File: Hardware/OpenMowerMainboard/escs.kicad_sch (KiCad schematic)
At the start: 46 parts, among them J15 Conn_02x02_Female, J24 Conn_01x06_Female, J25 Conn_02x02_Female, J26 Conn_01x06_Female, J27 Conn_02x02_Female, J28 Conn_01x05_Female, J29 Conn_01x05_Female, J30 Conn_01x09_Female, J31 Conn_02x02_Female, J32 Conn_01x06_Female, J33 Conn_02x02_Female, J34 Conn_01x06_Female, J35 Conn_02x02_Female, J36 Conn_01x05_Female, J37 Conn_01x05_Female, J38 Conn_01x09_Female, J39 Conn_02x02_Female, J40 Conn_01x06_Female, J41 Conn_02x02_Female, J42 Conn_01x06_Female, J43 Conn_02x02_Female, J44 Conn_01x05_Female, J45 Conn_01x05_Female, J46 Conn_01x09_Female, U4 xESC2, U5 xESC2, U6 xESC2

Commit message: BOM changes
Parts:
- C2, C3, C4, C6, C7, C8: Digikey (none) -> 399-6654-1-ND
- D10, D11, D12, D18, D19, D20, D4, D5, D6, D7, D8, D9, JP6, U4, U5, U6: DNP (none) -> Y
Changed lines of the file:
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@@
+      (effects (font (size 1.27 1.27)) hide)
+    )
+    (property "DNP" "Y" (id 5) (at 265.43 38.1 0)
       (effects (font (size 1.27 1.27)) hide)
     )
@@
     )
     (property "Config" "do not place" (id 4) (at 100.33 116.205 0)
+      (effects (font (size 1.27 1.27)) hide)
+    )
+    (property "DNP" "Y" (id 5) (at 100.33 116.205 0)
       (effects (font (size 1.27 1.27)) hide)
     )
@@
     )
     (property "Config" "do not place" (id 4) (at 255.905 38.1 0)
+      (effects (font (size 1.27 1.27)) hide)
+    )
+    (property "DNP" "Y" (id 5) (at 255.905 38.1 0)
       (effects (font (size 1.27 1.27)) hide)
     )
@@
       (effects (font (size 1.27 1.27)) hide)
     )
+    (property "DNP" "Y" (id 5) (at 133.35 38.1 0)
+      (effects (font (size 1.27 1.27)) hide)
+    )
     (pin "1")
     (pin "2")
@@
       (effects (font (size 1.27 1.27)) hide)
     )
+    (property "Digikey" "399-6654-1-ND" (id 7) (at 189.865 41.91 0)
+      (effects (font (size 1.27 1.27)) hide)
+    )
     (pin "1")
     (pin "2")
@@
     )
     (property "Config" "do not place" (id 4) (at 231.14 68.58 0)
+      (effects (font (size 1.27 1.27)) hide)
+    )
+    (property "DNP" "Y" (id 5) (at 231.14 68.58 0)
       (effects (font (size 1.27 1.27)) hide)
     )
@@
       (effects (font (size 1.27 1.27)) hide)
     )
+    (property "DNP" "Y" (id 5) (at 114.3 38.1 0)
+      (effects (font (size 1.27 1.27)) hide)
+    )
     (pin "1")
     (pin "2")
@@
       (effects (font (size 1.27 1.27)) hide)
     )
+    (property "DNP" "Y" (id 5) (at 36.195 99.695 0)
+      (effects (font (size 1.27 1.27)) hide)
+    )
     (pin "1")
     (pin "2")
@@
       (effects (font (size 1.27 1.27)) hide)
     )
+    (property "DNP" "Y" (id 5) (at 123.825 38.1 0)
+      (effects (font (size 1.27 1.27)) hide)
+    )
     (pin "1")
     (pin "2")
@@
     )
     (property "Config" "do not place" (id 4) (at 183.515 123.19 0)
+      (effects (font (size 1.27 1.27)) hide)
+    )
+    (property "DNP" "Y" (id 5) (at 183.515 123.19 0)
       (effects (font (size 1.27 1.27)) hide)
     )
@@
     )
     (property "Config" "do not place" (id 4) (at 88.9 68.58 0)
+      (effects (font (size 1.27 1.27)) hide)
+    )
+    (property "DNP" "Y" (id 5) (at 88.9 68.58 0)
       (effects (font (size 1.27 1.27)) hide)
     )
@@
       (effects (font (size 1.27 1.27)) hide)
     )
+    (property "DNP" "Y" (id 5) (at 156.21 153.67 0)
+      (effects (font (size 1.27 1.27)) hide)
+    )
     (pin "1")
     (pin "10")
@@
       (effects (font (size 1.27 1.27)) hide)
     )
+    (property "DNP" "Y" (id 5) (at 202.565 123.19 0)
+      (effects (font (size 1.27 1.27)) hide)
+    )
     (pin "1")
     (pin "2")
@@
       (effects (font (size 1.27 1.27)) hide)
     )
+    (property "DNP" "Y" (id 5) (at 274.955 38.1 0)
+      (effects (font (size 1.27 1.27)) hide)
+    )
     (pin "1")
     (pin "2")
@@
     )
     (property "Stock_PN" "CP-TH-220uF-63V" (id 6) (at 120.015 128.27 0)
+      (effects (font (size 1.27 1.27)) hide)
+    )
+    (property "Digikey" "399-6654-1-ND" (id 7) (at 120.015 128.27 0)
       (effects (font (size 1.27 1.27)) hide)
     )
@@
       (effects (font (size 1.27 1.27)) hide)
     )
+    (property "Digikey" "399-6654-1-ND" (id 7) (at 195.58 41.275 0)
+      (effects (font (size 1.27 1.27)) hide)
+    )
     (pin "1")
     (pin "2")
@@
     )
     (property "Stock_PN" "CP-TH-220uF-63V" (id 6) (at 47.625 45.085 0)
+      (effects (font (size 1.27 1.27)) hide)
+    )
+    (property "Digikey" "399-6654-1-ND" (id 7) (at 47.625 45.085 0)
       (effects (font (size 1.27 1.27)) hide)
     )
@@
     )
     (property "Config" "do not place" (id 4) (at 175.26 31.115 0)
+      (effects (font (size 1.27 1.27)) hide)
+    )
+    (property "DNP" "Y" (id 5) (at 175.26 31.115 0)
       (effects (font (size 1.27 1.27)) hide)
     )
@@
       (effects (font (size 1.27 1.27)) hide)
     )
+    (property "DNP" "Y" (id 5) (at 32.385 31.115 0)
+      (effects (font (size 1.27 1.27)) hide)
+    )
     (pin "1")
     (pin "2")
@@
     )
     (property "Stock_PN" "CP-TH-220uF-63V" (id 6) (at 114.3 128.905 0)
+      (effects (font (size 1.27 1.27)) hide)
+    )
+    (property "Digikey" "399-6654-1-ND" (id 7) (at 114.3 128.905 0)
       (effects (font (size 1.27 1.27)) hide)
     )
@@
       (effects (font (size 1.27 1.27)) hide)
     )
+    (property "DNP" "Y" (id 5) (at 193.04 123.19 0)
+      (effects (font (size 1.27 1.27)) hide)
+    )
     (pin "1")
     (pin "2")
@@
       (effects (font (size 1.27 1.27)) hide)
     )
+    (property "Digikey" "399-6654-1-ND" (id 7) (at 53.34 45.085 0)
+      (effects (font (size 1.27 1.27)) hide)
+    )

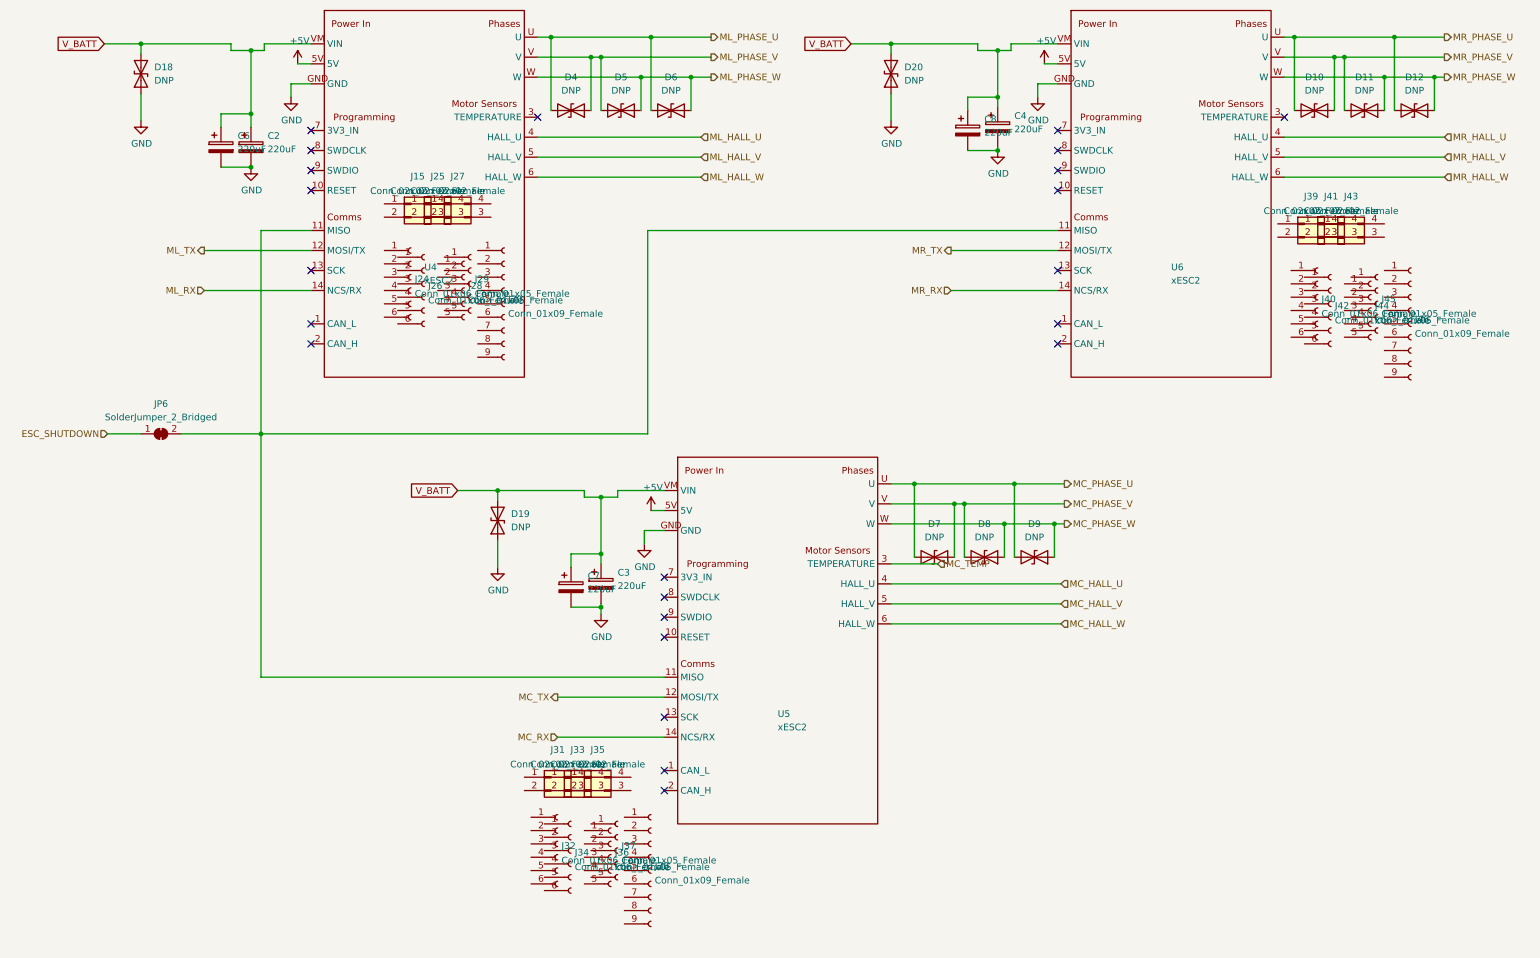
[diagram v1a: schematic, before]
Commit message: fix: fixed ERC/DRC errors, removed LM2596S
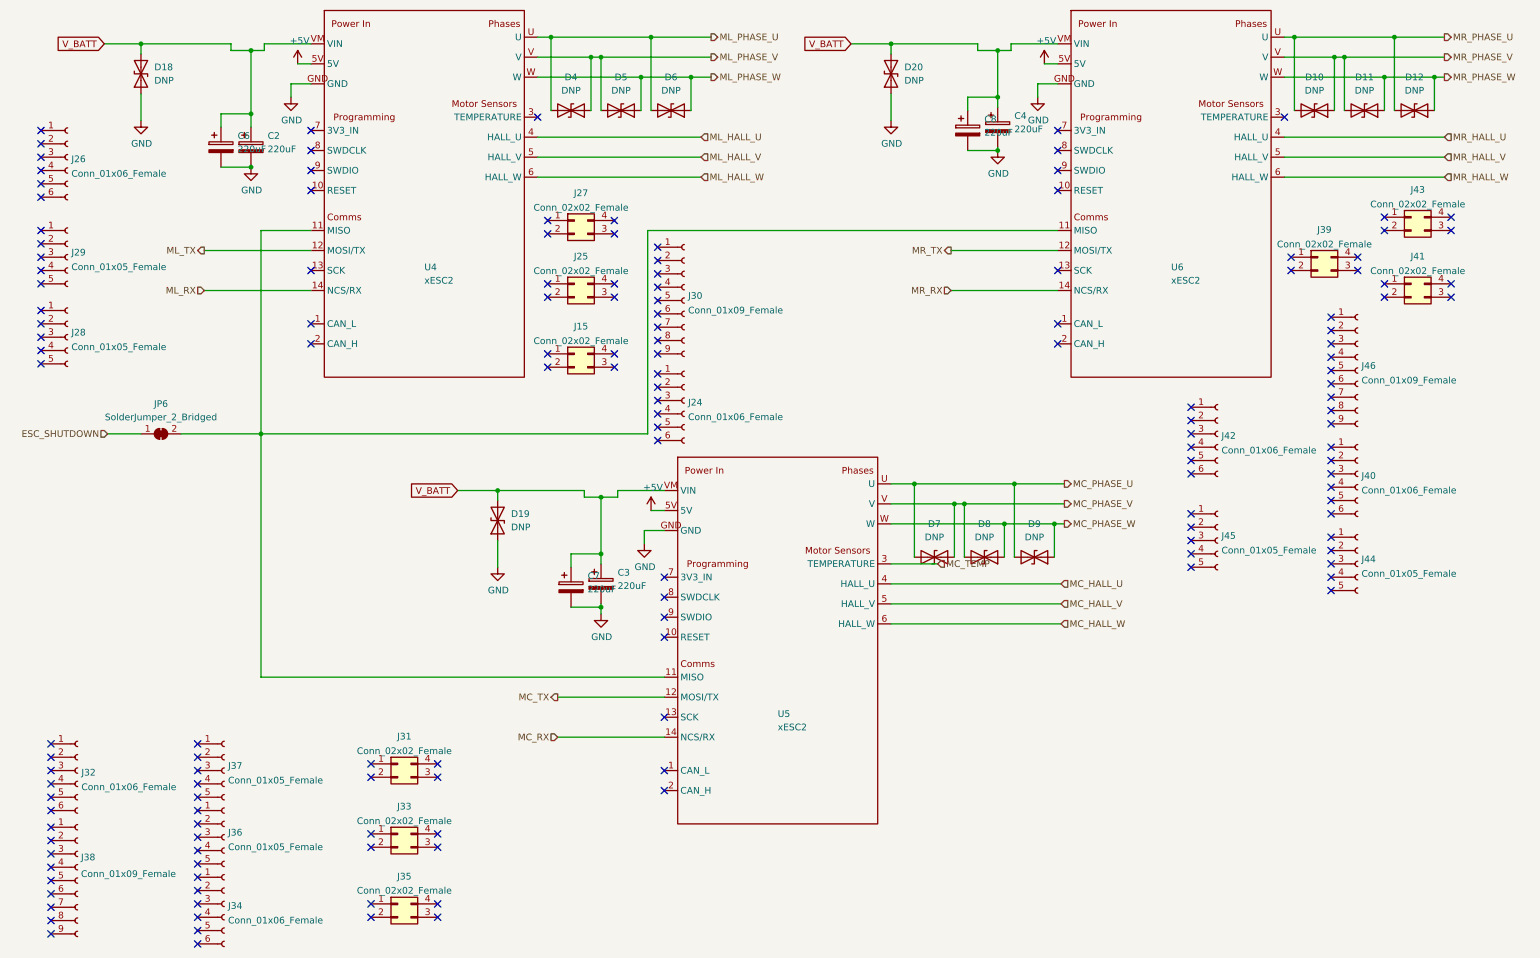
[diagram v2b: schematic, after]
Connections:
- no-connect marks 23 -> 152
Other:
- moved on the sheet: J15, J24, J25, J26, J27, J28, J29, J30, J31, J32, J33, J34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

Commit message: feat: remove C4 from board (no space)
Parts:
- C4: now left out of the parts list
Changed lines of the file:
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@@
   )
   (symbol (lib_id "Device:C_Polarized") (at 195.58 41.275 0) (unit 1)
-    (in_bom yes) (on_board yes) (fields_autoplaced)
+    (in_bom no) (on_board no) (fields_autoplaced)
     (property "Reference" "C4" (id 0) (at 198.755 39.1159 0)
       (effects (font (size 1.27 1.27)) (justify left))

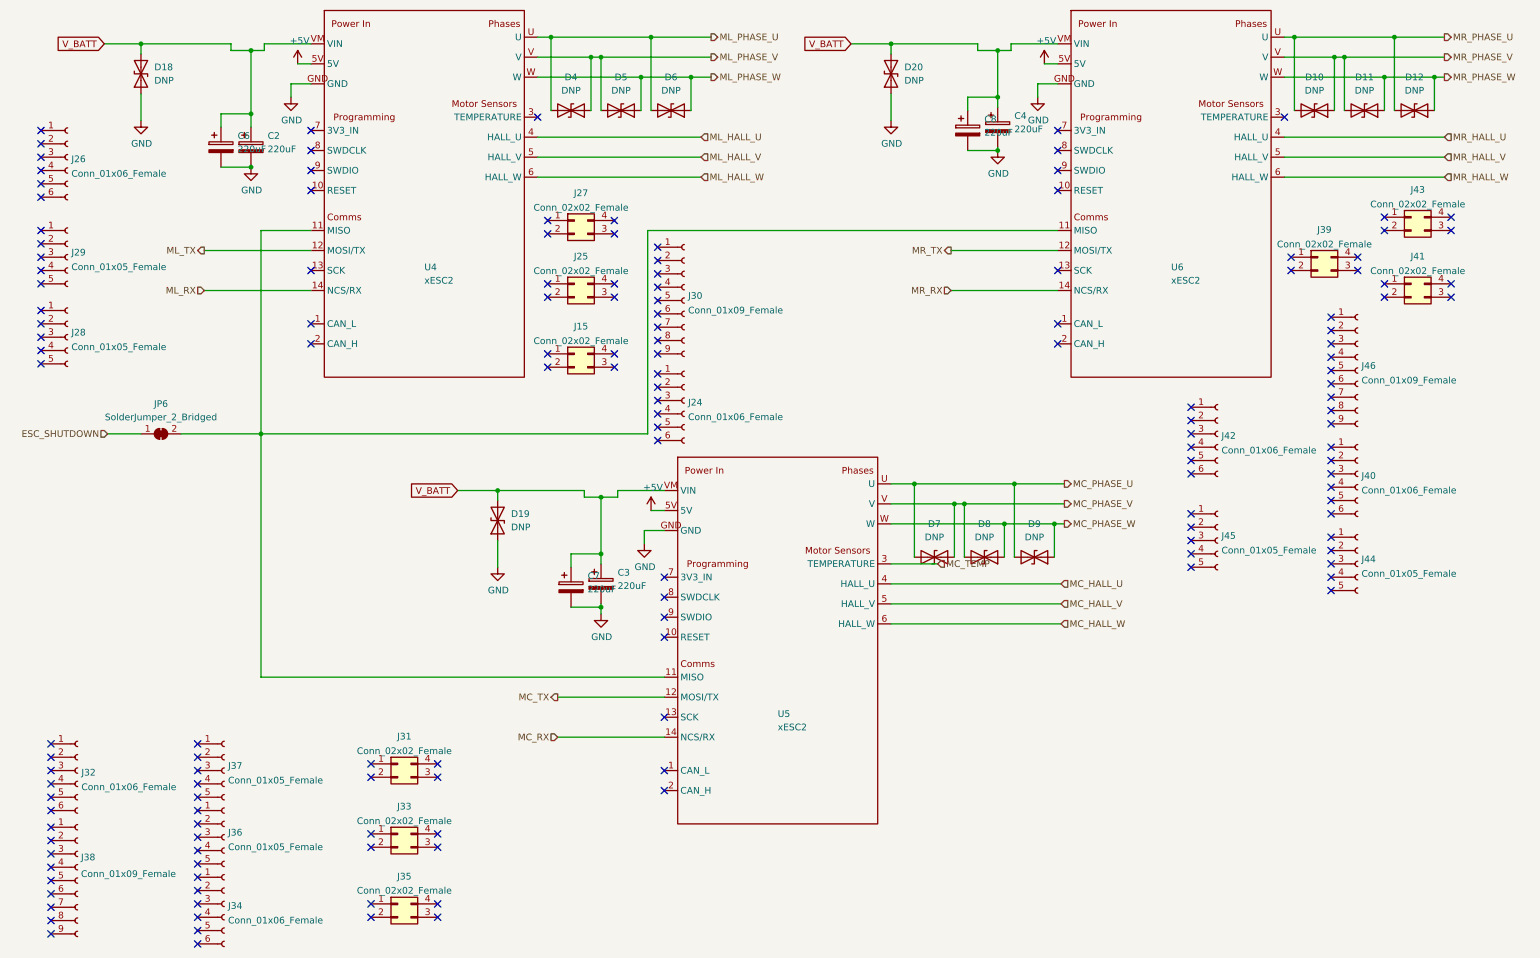
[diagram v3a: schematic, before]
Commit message: fix: exclude C3, C6 from BOM
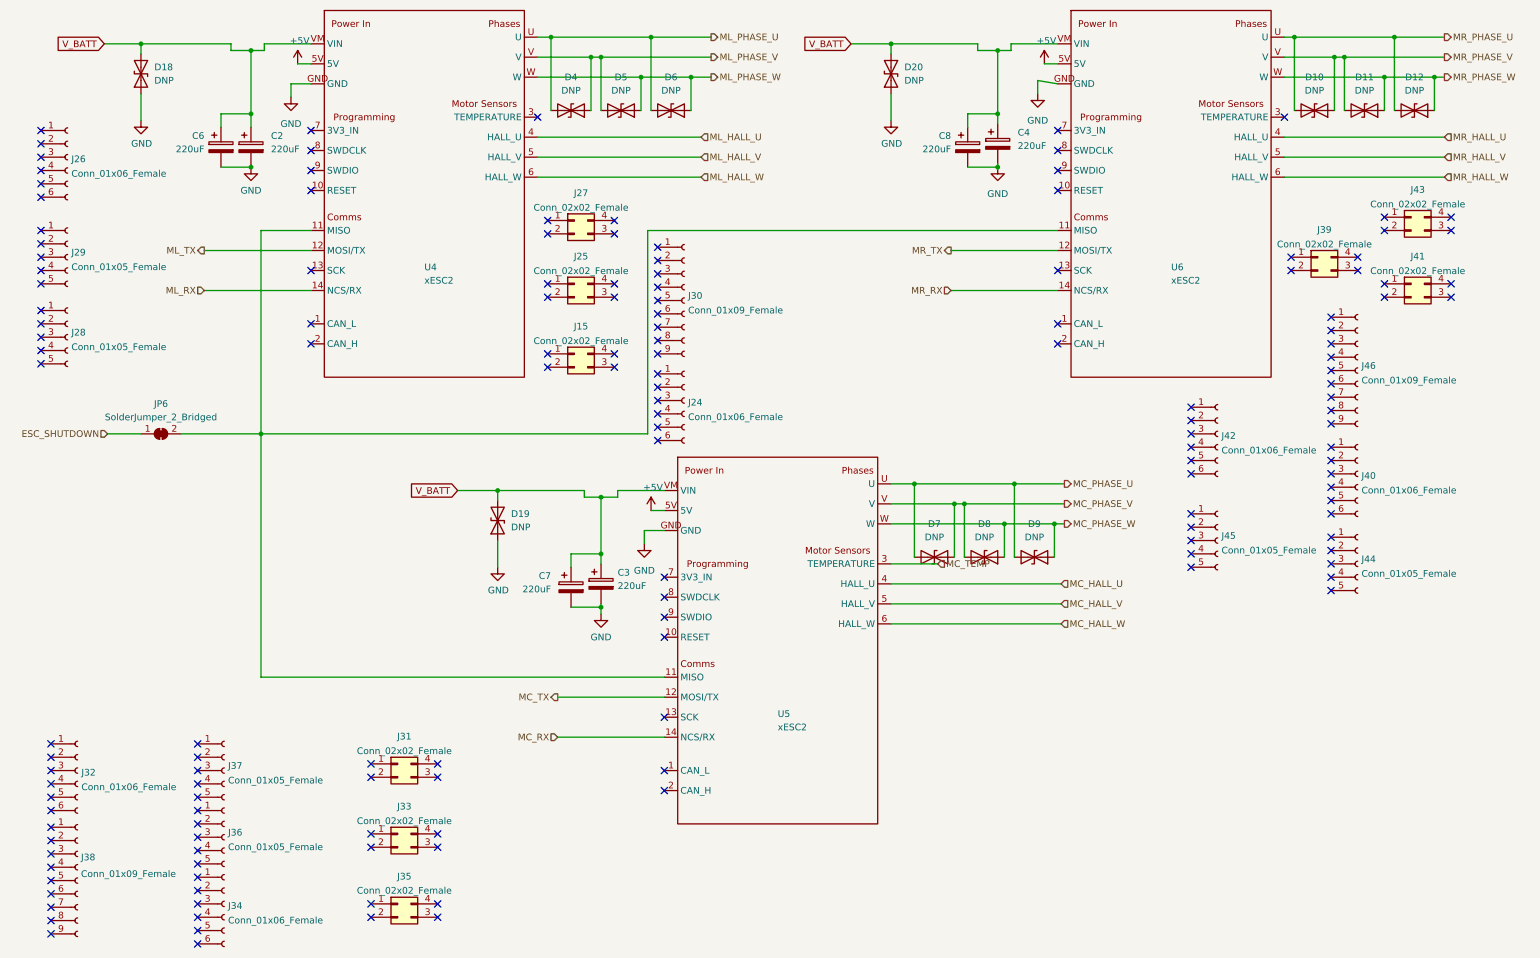
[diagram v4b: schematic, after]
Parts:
- C3, C6: now left out of the parts list
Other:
- moved on the sheet: C4, C8

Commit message: feat(bom): update LCSC codes
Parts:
- C3, C4, C6: Config (none) -> do not place
- J15, J25, J27, J31, J33, J35, J39, J41, J43: LCSC C239342 -> C2935982
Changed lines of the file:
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@@
       (effects (font (size 1.27 1.27)) hide)
     )
-    (property "LCSC" "C239342" (id 4) (at 81.28 162.56 0)
+    (property "LCSC" "C2935982" (id 4) (at 81.28 162.56 0)
       (effects (font (size 1.27 1.27)) hide)
     )
@@
       (effects (font (size 1.27 1.27)) hide)
     )
-    (property "LCSC" "C239342" (id 4) (at 114.935 84.455 0)
+    (property "LCSC" "C2935982" (id 4) (at 114.935 84.455 0)
       (effects (font (size 1.27 1.27)) hide)
     )
@@
       (effects (font (size 1.27 1.27)) hide)
     )
-    (property "LCSC" "C239342" (id 4) (at 274.32 58.42 0)
+    (property "LCSC" "C2935982" (id 4) (at 274.32 58.42 0)
       (effects (font (size 1.27 1.27)) hide)
     )
@@
       (effects (font (size 1.27 1.27)) hide)
     )
-    (property "LCSC" "C239342" (id 4) (at 274.32 71.12 0)
+    (property "LCSC" "C2935982" (id 4) (at 274.32 71.12 0)
       (effects (font (size 1.27 1.27)) hide)
     )
@@
       (effects (font (size 1.27 1.27)) hide)
     )
-    (property "LCSC" "C239342" (id 4) (at 114.935 71.12 0)
+    (property "LCSC" "C2935982" (id 4) (at 114.935 71.12 0)
       (effects (font (size 1.27 1.27)) hide)
     )
@@
       (effects (font (size 1.27 1.27)) hide)
     )
+    (property "Config" "do not place" (id 8) (at 120.015 128.27 0)
+      (effects (font (size 1.27 1.27)) hide)
+    )
     (pin "1")
     (pin "2")
@@
       (effects (font (size 1.27 1.27)) hide)
     )
-    (property "LCSC" "C239342" (id 4) (at 256.54 66.04 0)
+    (property "LCSC" "C2935982" (id 4) (at 256.54 66.04 0)
       (effects (font (size 1.27 1.27)) hide)
     )
@@
     )
     (property "Digikey" "399-6654-1-ND" (id 7) (at 195.58 44.45 0)
+      (effects (font (size 1.27 1.27)) hide)
+    )
+    (property "Config" "do not place" (id 8) (at 195.58 44.45 0)
       (effects (font (size 1.27 1.27)) hide)
     )
@@
       (effects (font (size 1.27 1.27)) hide)
     )
+    (property "Config" "do not place" (id 8) (at 47.625 45.085 0)
+      (effects (font (size 1.27 1.27)) hide)
+    )
     (pin "1")
     (pin "2")
@@
       (effects (font (size 1.27 1.27)) hide)
     )
-    (property "LCSC" "C239342" (id 4) (at 81.28 175.895 0)
+    (property "LCSC" "C2935982" (id 4) (at 81.28 175.895 0)
       (effects (font (size 1.27 1.27)) hide)
     )
@@
       (effects (font (size 1.27 1.27)) hide)
     )
-    (property "LCSC" "C239342" (id 4) (at 114.935 59.055 0)
+    (property "LCSC" "C2935982" (id 4) (at 114.935 59.055 0)
       (effects (font (size 1.27 1.27)) hide)
     )
@@
       (effects (font (size 1.27 1.27)) hide)
     )
-    (property "LCSC" "C239342" (id 4) (at 81.28 189.23 0)
-      (effects (font (size 1.27 1.27)) hide)
-    )
+    (property "LCSC" "C2935982" (id 4) (at 81.28 189.23 0)
+      (effects (font (size 1.27 1.27)) hide)
+    )
